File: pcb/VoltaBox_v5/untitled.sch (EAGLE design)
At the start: 64 parts, among them J1 0, X1 112J-TDAR-R(MICROSD), X2 52892-0895, X3 52892-0895, X4 XT30PW-F, X6 XT60PW-M, X7 KLS1-233

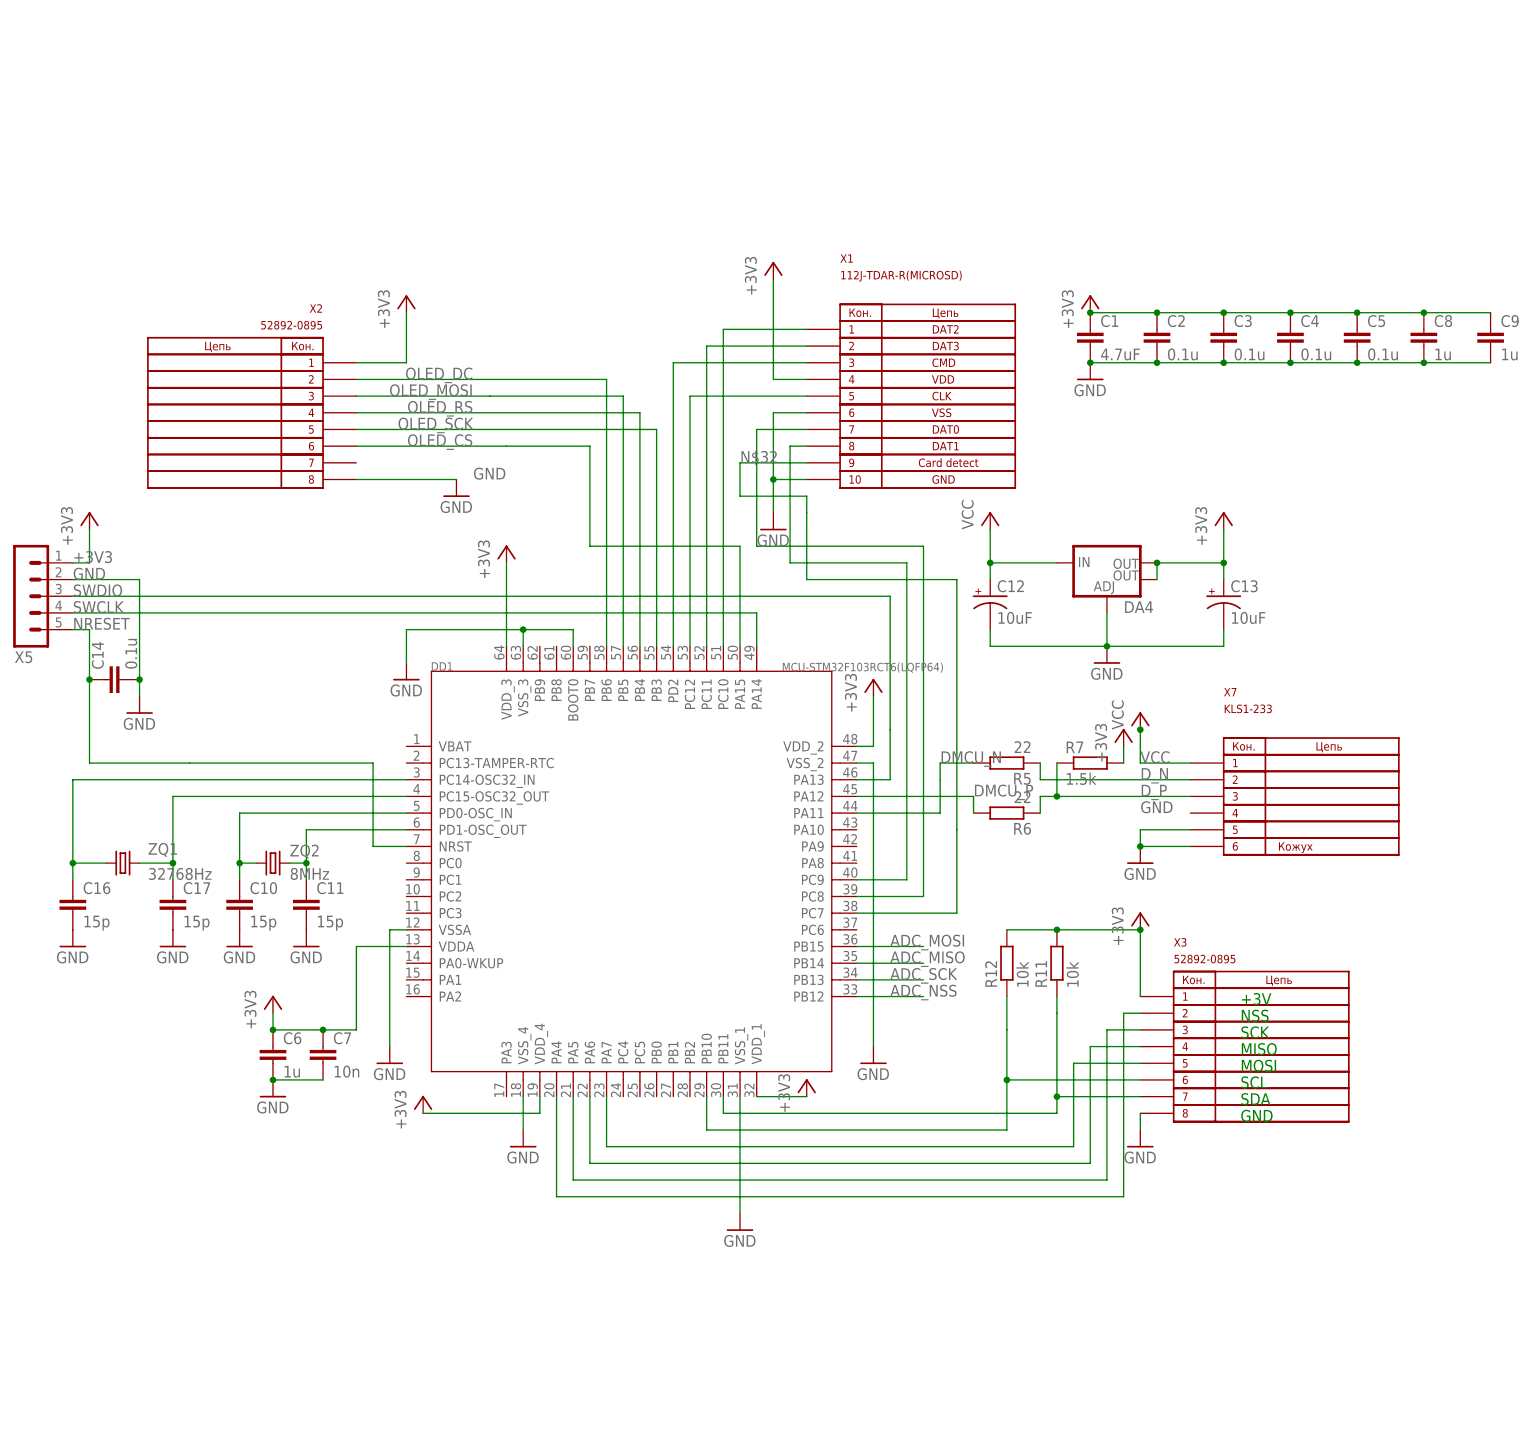
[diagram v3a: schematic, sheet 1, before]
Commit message: additional oled connector added, some small fixes, swd relayout
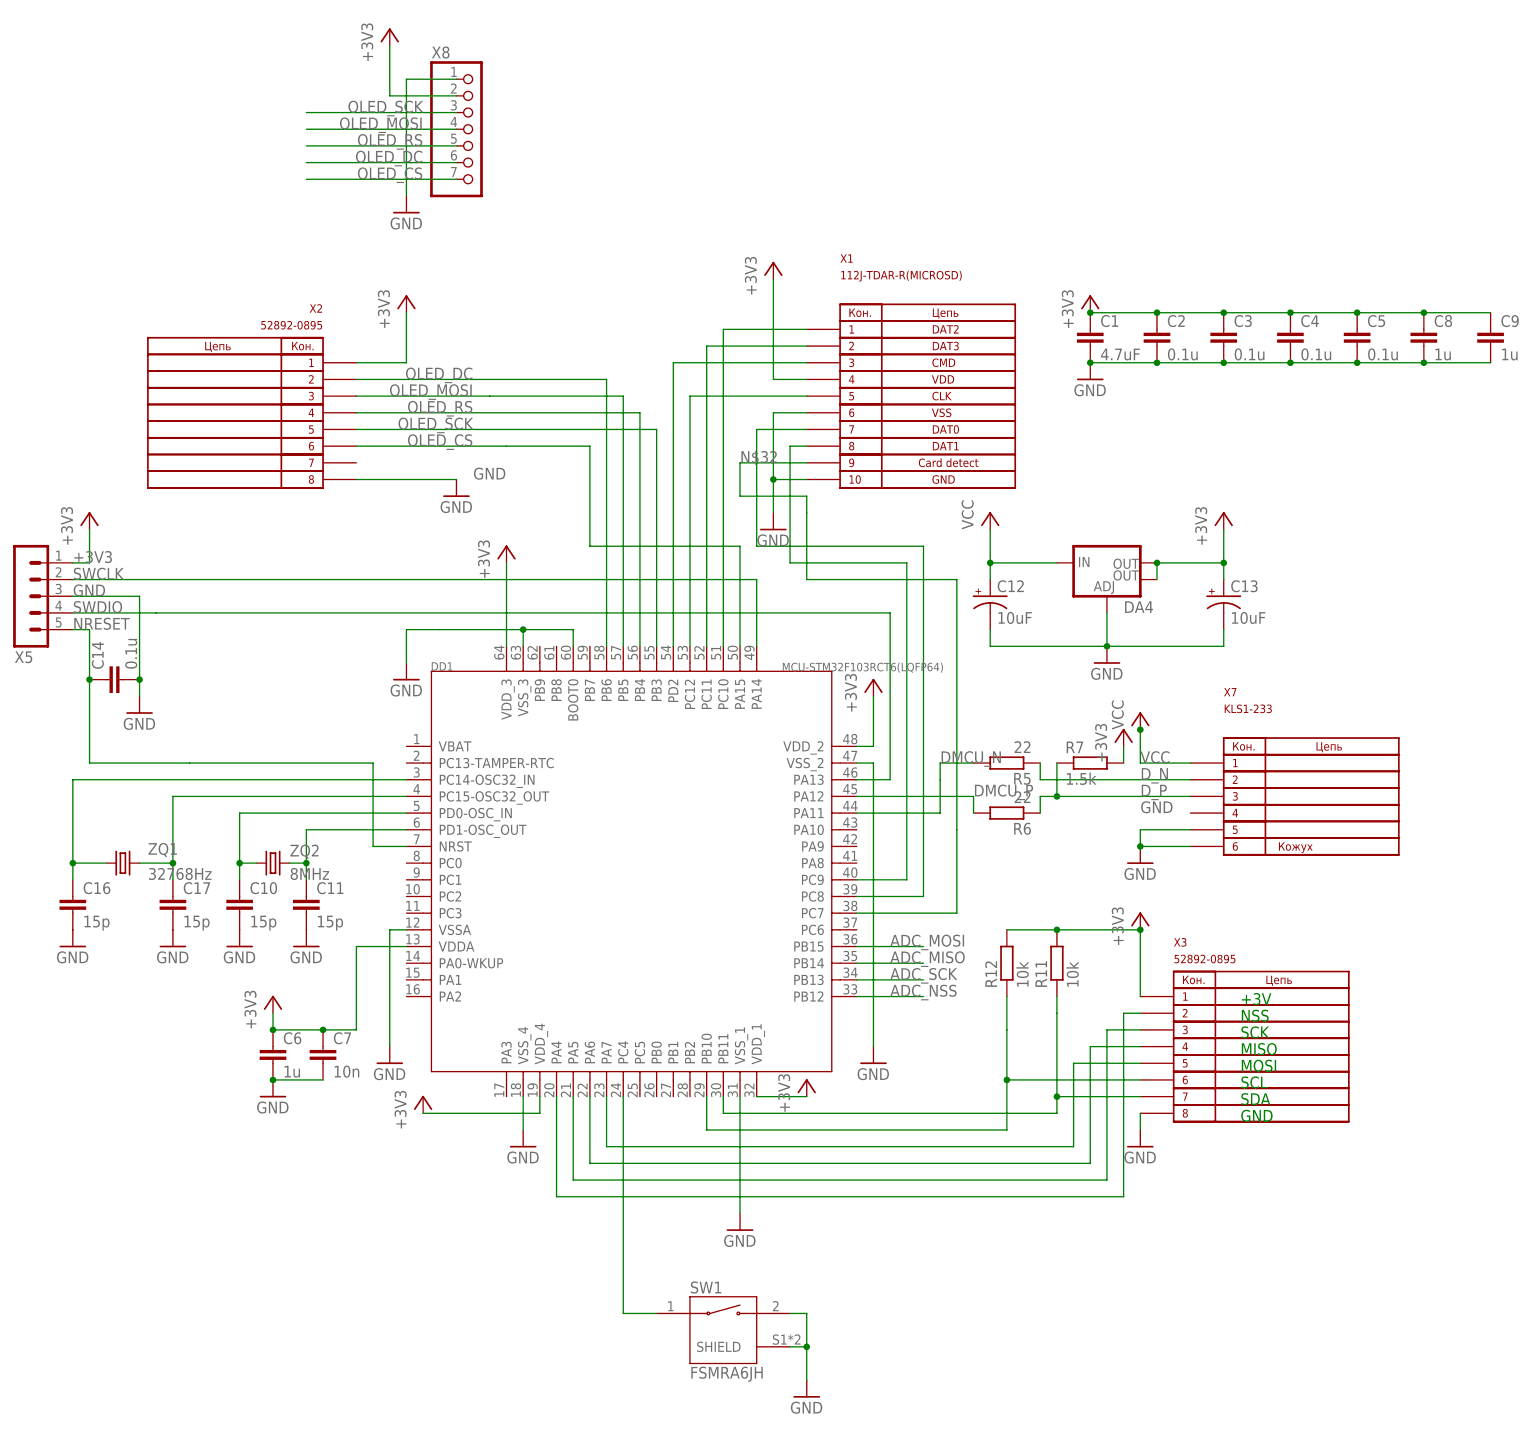
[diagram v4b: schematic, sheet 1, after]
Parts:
- removed TP1, TP2, TP3: TPSQB1,27, testpad:TPSQB1,27
- added SW1: FSMRA6JH, FSMRA6JH:FSMRA6JH
- added X8: (no value), pinhead:PINHD-1X7
- R2: value 3.3K -> 2.7K
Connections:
- new net N$17: DD1.PC4, SW1.1
- net +3V3: now also X8.2
- net +4V: no longer TP1.TP, TP2.TP, TP3.TP
- net GND: now also SW1.2, SW1.SHIELD, X5.3, X8.1; no longer X5.2
- net OLED_CS: now also X8.7
- net OLED_DC: now also X8.6
- net OLED_MOSI: now also X8.4
- net OLED_RS: now also X8.5
- net OLED_SCK: now also X8.3
- net SWCLK: now also X5.2; no longer X5.4
- net SWDIO: now also X5.4; no longer X5.3
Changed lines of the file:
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@@
 <part name="ZQ2" library="crystal" library_urn="urn:adsk.eagle:library:204" deviceset="CRYSTAL" device="HC49UP" package3d_urn="urn:adsk.eagle:package:12078/1" value="8MHz"/>
 <part name="ZQ1" library="crystal-geyer_V1_0" library_urn="urn:adsk.eagle:library:203" deviceset="KX-327" device="-NHT" package3d_urn="urn:adsk.eagle:package:11937/1" value="32768Hz"/>
-<part name="R2" library="resistor" library_urn="urn:adsk.eagle:library:348" deviceset="R-EU_" device="R0603" package3d_urn="urn:adsk.eagle:package:26057/1" value="3.3K"/>
+<part name="R2" library="resistor" library_urn="urn:adsk.eagle:library:348" deviceset="R-EU_" device="R0603" package3d_urn="urn:adsk.eagle:package:26057/1" value="2.7K"/>
 <part name="C27" library="eagle-ltspice" library_urn="urn:adsk.eagle:library:217" deviceset="C" device="C0603" package3d_urn="urn:adsk.eagle:package:13262/1" value="10p"/>
 <part name="C28" library="eagle-ltspice" library_urn="urn:adsk.eagle:library:217" deviceset="C" device="C0603" package3d_urn="urn:adsk.eagle:package:13262/1" value="0.1u"/>
@@
 <part name="J1" library="rcl" library_urn="urn:adsk.eagle:library:334" deviceset="R-EU_" device="R2010" package3d_urn="urn:adsk.eagle:package:23551/2" value="0"/>
 <part name="X7" library="untitled" deviceset="KLS1-233" device=""/>
-<part name="TP1" library="testpad" library_urn="urn:adsk.eagle:library:385" deviceset="TPSQ" device="B1,27" package3d_urn="urn:adsk.eagle:package:27944/1"/>
-<part name="TP2" library="testpad" library_urn="urn:adsk.eagle:library:385" deviceset="TPSQ" device="B1,27" package3d_urn="urn:adsk.eagle:package:27944/1"/>
-<part name="TP3" library="testpad" library_urn="urn:adsk.eagle:library:385" deviceset="TPSQ" device="B1,27" package3d_urn="urn:adsk.eagle:package:27944/1"/>
 <part name="U$3" library="untitled" deviceset="GND2" device=""/>
 <part name="U$9" library="untitled" deviceset="GND2" device=""/>
@@
 <part name="C24" library="eagle-ltspice" library_urn="urn:adsk.eagle:library:217" deviceset="C" device="C0603" package3d_urn="urn:adsk.eagle:package:13262/1" value="0.1u"/>
 <part name="U$20" library="untitled" deviceset="GND2" device=""/>
+<part name="X8" library="pinhead" library_urn="urn:adsk.eagle:library:325" deviceset="PINHD-1X7" device="" package3d_urn="urn:adsk.eagle:package:22477/2"/>
+<part name="+3V3" library="supply1" library_urn="urn:adsk.eagle:library:371" deviceset="+3V3" device=""/>
+<part name="GND4" library="supply1" library_urn="urn:adsk.eagle:library:371" deviceset="GND" device=""/>
+<part name="SW1" library="FSMRA6JH" deviceset="FSMRA6JH" device=""/>
+<part name="GND18" library="supply1" library_urn="urn:adsk.eagle:library:371" deviceset="GND" device=""/>
 </parts>
 <sheets>
@@
 <instance part="X7" gate="G$1" x="165.1" y="78.74"/>
 <instance part="C17" gate="G$1" x="-10.16" y="63.5"/>
+<instance part="X8" gate="A" x="35.56" y="180.34"/>
+<instance part="+3V3" gate="G$1" x="22.86" y="195.58"/>
+<instance part="GND4" gate="1" x="25.4" y="167.64"/>
+<instance part="SW1" gate="G$1" x="73.66" y="-2.54"/>
+<instance part="GND18" gate="1" x="86.36" y="-12.7"/>
 </instances>
 <busses>
@@
 <segment>
 <pinref part="GND5" gate="1" pin="GND"/>
-<pinref part="X5" gate="G$1" pin="2"/>
 <wire x1="-15.24" y1="93.98" x2="-15.24" y2="96.52" width="0.1524" layer="91"/>
-<wire x1="-15.24" y1="96.52" x2="-15.24" y2="111.76" width="0.1524" layer="91"/>
-<wire x1="-15.24" y1="111.76" x2="-25.4" y2="111.76" width="0.1524" layer="91"/>
+<wire x1="-15.24" y1="96.52" x2="-15.24" y2="109.22" width="0.1524" layer="91"/>
 <pinref part="C14" gate="G$1" pin="2"/>
 <junction x="-15.24" y="96.52"/>
-<label x="-25.4" y="111.76" size="1.778" layer="95"/>
+<label x="-25.4" y="109.22" size="1.778" layer="95"/>
+<pinref part="X5" gate="G$1" pin="3"/>
+<wire x1="-25.4" y1="109.22" x2="-15.24" y2="109.22" width="0.1524" layer="91"/>
 </segment>
 <segment>
@@
 <pinref part="GND12" gate="1" pin="GND"/>
 </segment>
+<segment>
+<pinref part="X8" gate="A" pin="1"/>
+<wire x1="33.02" y1="187.96" x2="25.4" y2="187.96" width="0.1524" layer="91"/>
+<pinref part="GND4" gate="1" pin="GND"/>
+<wire x1="25.4" y1="187.96" x2="25.4" y2="170.18" width="0.1524" layer="91"/>
+</segment>
+<segment>
+<pinref part="SW1" gate="G$1" pin="2"/>
+<wire x1="83.82" y1="0" x2="86.36" y2="0" width="0.1524" layer="91"/>
+<pinref part="GND18" gate="1" pin="GND"/>
+<wire x1="86.36" y1="0" x2="86.36" y2="-5.08" width="0.1524" layer="91"/>
+<pinref part="SW1" gate="G$1" pin="SHIELD"/>
+<wire x1="86.36" y1="-5.08" x2="86.36" y2="-10.16" width="0.1524" layer="91"/>
+<wire x1="83.82" y1="-5.08" x2="86.36" y2="-5.08" width="0.1524" layer="91"/>
+<junction x="86.36" y="-5.08"/>
+</segment>
 </net>
 <net name="VCC" class="0">
@@
 <wire x1="134.62" y1="86.36" x2="134.62" y2="83.82" width="0.1524" layer="91"/>
 </segment>
+<segment>
+<pinref part="X8" gate="A" pin="2"/>
+<wire x1="33.02" y1="185.42" x2="22.86" y2="185.42" width="0.1524" layer="91"/>
+<pinref part="+3V3" gate="G$1" pin="+3V3"/>
+<wire x1="22.86" y1="185.42" x2="22.86" y2="193.04" width="0.1524" layer="91"/>
+</segment>
 </net>
 <net name="SWDIO" class="0">
@@
 <pinref part="DD1" gate="G$1" pin="PA13"/>
 <wire x1="93.98" y1="81.28" x2="99.06" y2="81.28" width="0.1524" layer="91"/>
-<wire x1="99.06" y1="81.28" x2="99.06" y2="88.9" width="0.1524" layer="91"/>
-<pinref part="X5" gate="G$1" pin="3"/>
-<wire x1="99.06" y1="88.9" x2="99.06" y2="109.22" width="0.1524" layer="91"/>
-<wire x1="99.06" y1="109.22" x2="-25.4" y2="109.22" width="0.1524" layer="91"/>
-<label x="-25.4" y="109.22" size="1.778" layer="95"/>
+<wire x1="99.06" y1="81.28" x2="99.06" y2="106.68" width="0.1524" layer="91"/>
+<wire x1="99.06" y1="106.68" x2="-12.7" y2="106.68" width="0.1524" layer="91"/>
+<label x="-25.4" y="106.68" size="1.778" layer="95"/>
+<pinref part="X5" gate="G$1" pin="4"/>
+<wire x1="-25.4" y1="106.68" x2="-12.7" y2="106.68" width="0.1524" layer="91"/>
 </segment>
 </net>
 <net name="SWCLK" class="0">
 <segment>
-<pinref part="X5" gate="G$1" pin="4"/>
-<wire x1="-25.4" y1="106.68" x2="78.74" y2="106.68" width="0.1524" layer="91"/>
 <pinref part="DD1" gate="G$1" pin="PA14"/>
-<wire x1="78.74" y1="106.68" x2="78.74" y2="101.6" width="0.1524" layer="91"/>
-<label x="-25.4" y="106.68" size="1.778" layer="95"/>
+<wire x1="-25.4" y1="111.76" x2="78.74" y2="111.76" width="0.1524" layer="91"/>
+<wire x1="78.74" y1="111.76" x2="78.74" y2="101.6" width="0.1524" layer="91"/>
+<label x="-25.4" y="111.76" size="1.778" layer="95"/>
+<pinref part="X5" gate="G$1" pin="2"/>
 </segment>
 </net>
@@
 <pinref part="X2" gate="G$1" pin="P$5"/>
 </segment>
+<segment>
+<wire x1="10.16" y1="182.88" x2="33.02" y2="182.88" width="0.1524" layer="91"/>
+<label x="27.94" y="182.88" size="1.778" layer="95" rot="MR0"/>
+<pinref part="X8" gate="A" pin="3"/>
+</segment>
 </net>
 <net name="OLED_CS" class="0">
@@
 <pinref part="X2" gate="G$1" pin="P$6"/>
 </segment>
+<segment>
+<wire x1="10.16" y1="172.72" x2="33.02" y2="172.72" width="0.1524" layer="91"/>
+<label x="27.94" y="172.72" size="1.778" layer="95" rot="MR0"/>
+<pinref part="X8" gate="A" pin="7"/>
+</segment>
 </net>
 <net name="OLED_DC" class="0">
@@
 <pinref part="DD1" gate="G$1" pin="PB6"/>
 <pinref part="X2" gate="G$1" pin="P$2"/>
+</segment>
+<segment>
+<wire x1="33.02" y1="175.26" x2="10.16" y2="175.26" width="0.1524" layer="91"/>
+<label x="27.94" y="175.26" size="1.778" layer="95" rot="MR0"/>
+<pinref part="X8" gate="A" pin="6"/>
 </segment>
 </net>
@@
 <wire x1="38.1" y1="139.7" x2="17.78" y2="139.7" width="0.1524" layer="91"/>
 </segment>
+<segment>
+<label x="27.94" y="180.34" size="1.778" layer="95" rot="MR0"/>
+<wire x1="33.02" y1="180.34" x2="10.16" y2="180.34" width="0.1524" layer="91"/>
+<pinref part="X8" gate="A" pin="4"/>
+</segment>
 </net>
 <net name="OLED_RS" class="0">
@@
 <wire x1="60.96" y1="137.16" x2="60.96" y2="101.6" width="0.1524" layer="91"/>
 <wire x1="17.78" y1="137.16" x2="60.96" y2="137.16" width="0.1524" layer="91"/>
+</segment>
+<segment>
+<label x="27.94" y="177.8" size="1.778" layer="95" rot="MR0"/>
+<wire x1="10.16" y1="177.8" x2="33.02" y2="177.8" width="0.1524" layer="91"/>
+<pinref part="X8" gate="A" pin="5"/>
 </segment>
 </net>
@@
 <wire x1="93.98" y1="60.96" x2="109.22" y2="60.96" width="0.1524" layer="91"/>
 <wire x1="109.22" y1="60.96" x2="109.22" y2="73.66" width="0.1524" layer="91"/>
+</segment>
+</net>
+<net name="N$17" class="0">
+<segment>
+<pinref part="DD1" gate="G$1" pin="PC4"/>
+<wire x1="58.42" y1="33.02" x2="58.42" y2="0" width="0.1524" layer="91"/>
+<pinref part="SW1" gate="G$1" pin="1"/>
+<wire x1="58.42" y1="0" x2="63.5" y2="0" width="0.1524" layer="91"/>
 </segment>
 </net>
@@
 <instance part="U$6" gate="G$1" x="142.24" y="25.4"/>
 <instance part="J1" gate="G$1" x="73.66" y="45.72"/>
-<instance part="TP1" gate="G$1" x="114.3" y="27.94"/>
-<instance part="TP2" gate="G$1" x="119.38" y="27.94"/>
-<instance part="TP3" gate="G$1" x="124.46" y="27.94"/>
 <instance part="U$3" gate="G$1" x="43.18" y="10.16"/>
 <instance part="U$9" gate="G$1" x="50.8" y="10.16"/>
@@
 <wire x1="78.74" y1="45.72" x2="93.98" y2="45.72" width="0.1524" layer="91"/>
 <junction x="101.6" y="45.72"/>
-<pinref part="TP1" gate="G$1" pin="TP"/>
 <wire x1="93.98" y1="45.72" x2="101.6" y2="45.72" width="0.1524" layer="91"/>
-<wire x1="101.6" y1="30.48" x2="114.3" y2="30.48" width="0.1524" layer="91"/>
-<pinref part="TP2" gate="G$1" pin="TP"/>
-<wire x1="119.38" y1="30.48" x2="114.3" y2="30.48" width="0.1524" layer="91"/>
-<junction x="114.3" y="30.48"/>
-<pinref part="TP3" gate="G$1" pin="TP"/>
-<wire x1="124.46" y1="30.48" x2="119.38" y2="30.48" width="0.1524" layer="91"/>
-<junction x="119.38" y="30.48"/>
 <pinref part="C22" gate="G$1" pin="2"/>
 <wire x1="93.98" y1="43.18" x2="93.98" y2="45.72" width="0.1524" layer="91"/>
